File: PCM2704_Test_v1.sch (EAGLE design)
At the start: 50 parts, among them IC1 REG1117, IC2 REG1117, X1 USB-MB-S

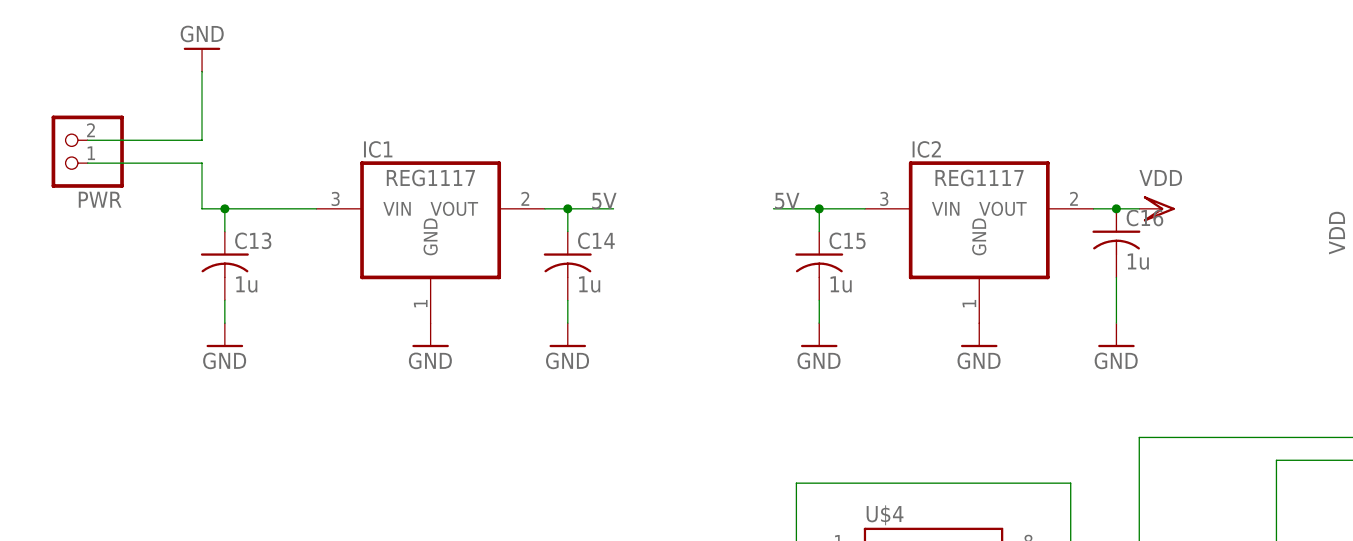
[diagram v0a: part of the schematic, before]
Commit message: Removed Voltage Regulators
For VBUS operation, no voltage regulators are required. I removed both
of them from the board along with all supporting components such as
filter caps, etc.
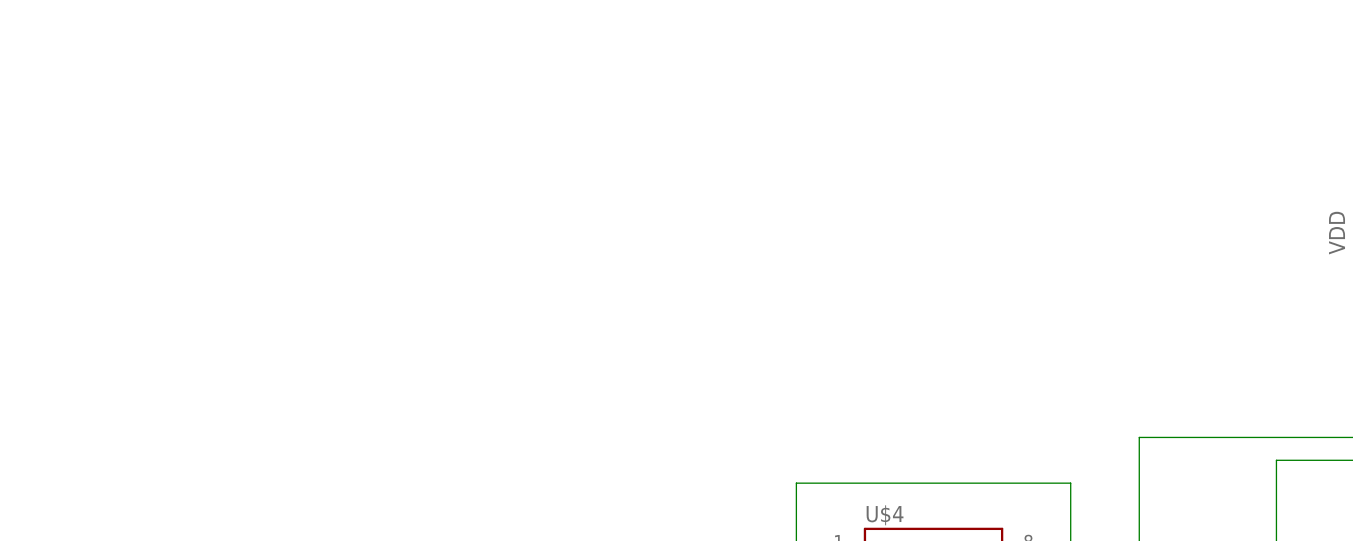
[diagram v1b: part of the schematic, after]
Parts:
- removed C13, C14, C15, C16: 1u, rcl:C-USC0805
- removed IC1, IC2: REG1117, burr-brown-3:REG1117
- removed PWR: (no value), pinhead:PINHD-1X2
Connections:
- removed net VIN: C13.1, IC1.VIN, PWR.1
- net 5V: no longer C14.1, C15.1, IC1.VOUT, IC2.VIN
- net GND: no longer C13.2, C14.2, C15.2, C16.2, IC1.GND, IC2.GND, PWR.2
- net VDD: no longer C16.1, IC2.VOUT
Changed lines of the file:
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@@
 <setting verticaltext="up"/>
 </settings>
-<grid distance="0.1" unitdist="inch" unit="inch" style="lines" multiple="1" display="yes" altdistance="0.01" altunitdist="inch" altunit="inch"/>
+<grid distance="0.1" unitdist="inch" unit="inch" style="lines" multiple="1" display="no" altdistance="0.01" altunitdist="inch" altunit="inch"/>
 <layers>
 <layer number="1" name="Top" color="4" fill="1" visible="no" active="no"/>
@@
 <part name="U$2" library="SparkFun-Connectors" deviceset="AUDIO-JACK3" device=""/>
 <part name="GND8" library="SparkFun" deviceset="GND" device=""/>
-<part name="GND9" library="SparkFun" deviceset="GND" device=""/>
-<part name="GND10" library="SparkFun" deviceset="GND" device=""/>
-<part name="C13" library="rcl" deviceset="C-US" device="C0805" value="1u"/>
-<part name="GND11" library="SparkFun" deviceset="GND" device=""/>
-<part name="C14" library="rcl" deviceset="C-US" device="C0805" value="1u"/>
-<part name="GND12" library="SparkFun" deviceset="GND" device=""/>
-<part name="IC1" library="burr-brown-3" deviceset="REG1117" device=""/>
-<part name="IC2" library="burr-brown-3" deviceset="REG1117" device=""/>
-<part name="C15" library="rcl" deviceset="C-US" device="C0805" value="1u"/>
-<part name="GND13" library="SparkFun" deviceset="GND" device=""/>
-<part name="GND14" library="SparkFun" deviceset="GND" device=""/>
-<part name="VDD1" library="supply1" deviceset="VDD" device=""/>
-<part name="C16" library="rcl" deviceset="C-US" device="C0805" value="1u"/>
-<part name="GND15" library="SparkFun" deviceset="GND" device=""/>
-<part name="PWR" library="pinhead" deviceset="PINHD-1X2" device=""/>
 <part name="L1" library="rcl" deviceset="L-US" device="L3225M"/>
 <part name="JPBUS" library="pinhead" deviceset="PINHD-1X2" device=""/>
@@
 <instance part="U$2" gate="G$1" x="198.12" y="15.24" rot="MR0"/>
 <instance part="GND8" gate="1" x="190.5" y="-2.54"/>
-<instance part="GND9" gate="1" x="-101.6" y="114.3"/>
-<instance part="GND10" gate="1" x="-127" y="147.32" rot="R180"/>
-<instance part="C13" gate="G$1" x="-124.46" y="124.46"/>
-<instance part="GND11" gate="1" x="-124.46" y="114.3"/>
-<instance part="C14" gate="G$1" x="-86.36" y="124.46"/>
-<instance part="GND12" gate="1" x="-86.36" y="114.3"/>
-<instance part="IC1" gate="G$1" x="-101.6" y="129.54"/>
-<instance part="IC2" gate="G$1" x="-40.64" y="129.54"/>
-<instance part="C15" gate="G$1" x="-58.42" y="124.46"/>
-<instance part="GND13" gate="1" x="-58.42" y="114.3"/>
-<instance part="GND14" gate="1" x="-40.64" y="114.3"/>
-<instance part="VDD1" gate="G$1" x="-20.32" y="129.54" rot="R270"/>
-<instance part="C16" gate="G$1" x="-25.4" y="127"/>
-<instance part="GND15" gate="1" x="-25.4" y="114.3"/>
-<instance part="PWR" gate="G$1" x="-142.24" y="137.16" rot="R180"/>
 <instance part="L1" gate="G$1" x="-101.6" y="43.18" rot="R90"/>
 <instance part="JPBUS" gate="G$1" x="-139.7" y="71.12" rot="R180"/>
@@
 </segment>
 <segment>
-<pinref part="GND9" gate="1" pin="GND"/>
-<pinref part="IC1" gate="G$1" pin="GND"/>
-</segment>
-<segment>
-<wire x1="-127" y1="137.16" x2="-127" y2="144.78" width="0.1524" layer="91"/>
-<pinref part="GND10" gate="1" pin="GND"/>
-<pinref part="PWR" gate="G$1" pin="2"/>
-<wire x1="-139.7" y1="137.16" x2="-127" y2="137.16" width="0.1524" layer="91"/>
-</segment>
-<segment>
-<pinref part="C13" gate="G$1" pin="2"/>
-<pinref part="GND11" gate="1" pin="GND"/>
-<wire x1="-124.46" y1="116.84" x2="-124.46" y2="119.38" width="0.1524" layer="91"/>
-</segment>
-<segment>
-<pinref part="C14" gate="G$1" pin="2"/>
-<pinref part="GND12" gate="1" pin="GND"/>
-<wire x1="-86.36" y1="116.84" x2="-86.36" y2="119.38" width="0.1524" layer="91"/>
-</segment>
-<segment>
-<pinref part="C15" gate="G$1" pin="2"/>
-<pinref part="GND13" gate="1" pin="GND"/>
-<wire x1="-58.42" y1="116.84" x2="-58.42" y2="119.38" width="0.1524" layer="91"/>
-</segment>
-<segment>
-<pinref part="IC2" gate="G$1" pin="GND"/>
-<pinref part="GND14" gate="1" pin="GND"/>
-</segment>
-<segment>
-<pinref part="C16" gate="G$1" pin="2"/>
-<pinref part="GND15" gate="1" pin="GND"/>
-<wire x1="-25.4" y1="116.84" x2="-25.4" y2="121.92" width="0.1524" layer="91"/>
-</segment>
-<segment>
 <pinref part="R2" gate="G$1" pin="2"/>
 <pinref part="GND16" gate="1" pin="GND"/>
@@
 </net>
 <net name="VDD" class="0">
-<segment>
-<pinref part="IC2" gate="G$1" pin="VOUT"/>
-<pinref part="VDD1" gate="G$1" pin="VDD"/>
-<wire x1="-22.86" y1="129.54" x2="-25.4" y2="129.54" width="0.1524" layer="91"/>
-<pinref part="C16" gate="G$1" pin="1"/>
-<wire x1="-25.4" y1="129.54" x2="-27.94" y2="129.54" width="0.1524" layer="91"/>
-<junction x="-25.4" y="129.54"/>
-</segment>
 <segment>
 <wire x1="12.7" y1="43.18" x2="-15.24" y2="43.18" width="0.1524" layer="91"/>
@@
 </segment>
 </net>
-<net name="VIN" class="0">
-<segment>
-<wire x1="-127" y1="134.62" x2="-127" y2="129.54" width="0.1524" layer="91"/>
-<wire x1="-127" y1="129.54" x2="-124.46" y2="129.54" width="0.1524" layer="91"/>
-<wire x1="-124.46" y1="129.54" x2="-114.3" y2="129.54" width="0.1524" layer="91"/>
-<pinref part="C13" gate="G$1" pin="1"/>
-<wire x1="-124.46" y1="127" x2="-124.46" y2="129.54" width="0.1524" layer="91"/>
-<junction x="-124.46" y="129.54"/>
-<pinref part="IC1" gate="G$1" pin="VIN"/>
-<pinref part="PWR" gate="G$1" pin="1"/>
-<wire x1="-139.7" y1="134.62" x2="-127" y2="134.62" width="0.1524" layer="91"/>
-</segment>
-</net>
 <net name="5V" class="0">
 <segment>
-<wire x1="-88.9" y1="129.54" x2="-86.36" y2="129.54" width="0.1524" layer="91"/>
-<pinref part="C14" gate="G$1" pin="1"/>
-<wire x1="-86.36" y1="129.54" x2="-81.28" y2="129.54" width="0.1524" layer="91"/>
-<wire x1="-86.36" y1="129.54" x2="-86.36" y2="127" width="0.1524" layer="91"/>
-<junction x="-86.36" y="129.54"/>
-<pinref part="IC1" gate="G$1" pin="VOUT"/>
-<label x="-83.82" y="129.54" size="1.778" layer="95"/>
-</segment>
-<segment>
-<pinref part="IC2" gate="G$1" pin="VIN"/>
-<wire x1="-63.5" y1="129.54" x2="-58.42" y2="129.54" width="0.1524" layer="91"/>
-<label x="-63.5" y="129.54" size="1.778" layer="95"/>
-<pinref part="C15" gate="G$1" pin="1"/>
-<wire x1="-58.42" y1="129.54" x2="-53.34" y2="129.54" width="0.1524" layer="91"/>
-<wire x1="-58.42" y1="127" x2="-58.42" y2="129.54" width="0.1524" layer="91"/>
-<junction x="-58.42" y="129.54"/>
-</segment>
-<segment>
 <pinref part="JPBUS" gate="G$1" pin="2"/>

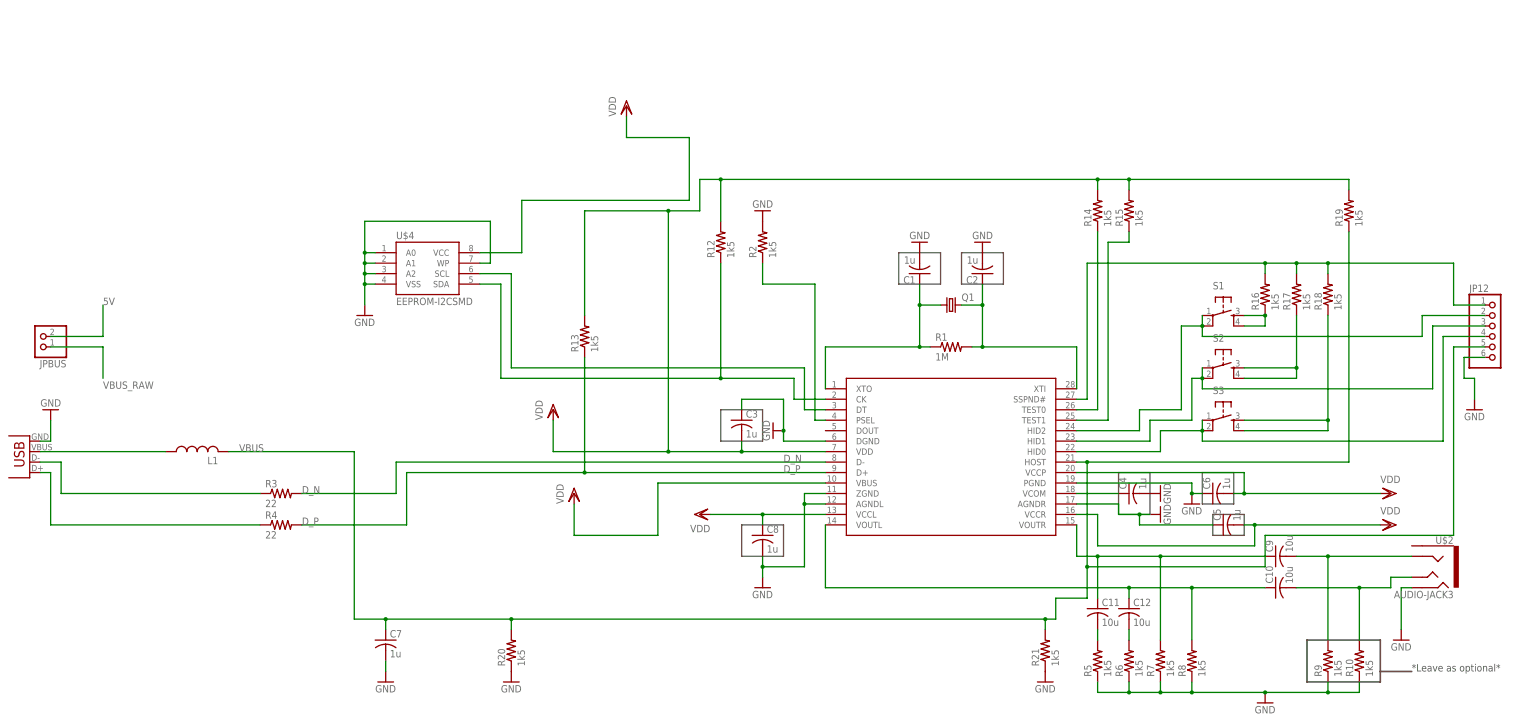
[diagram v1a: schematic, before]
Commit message: Removed unnecessary components
Removed:
-  Function Buttons
-  Resistors associated with the buttons

Moved some components around to make better use of the space on the
board. Decreased the board length and width. Routed the EEPROM traces
and added a bypass capacitor footprint to the power pin of the EEPROM.

Ripped up some traces and instead used polygon pours to route the
signals to make them lower impedance traces. This includes the traces
routed to the headphone jack and the USB VBUS pin.
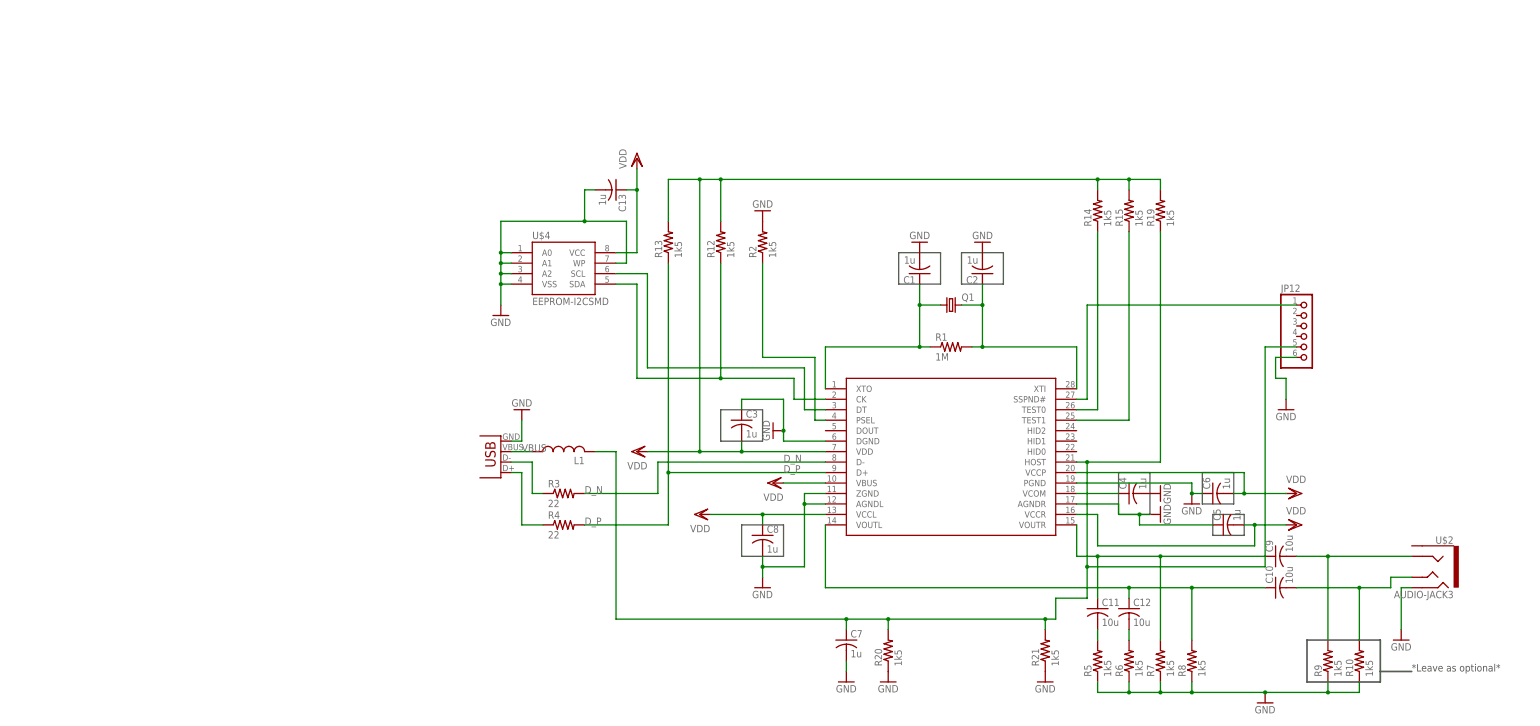
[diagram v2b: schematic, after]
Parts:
- removed JPBUS: (no value), pinhead:PINHD-1X2
- removed R16, R17, R18: 1k5, rcl:R-US_R0603
- removed S1, S2, S3: (no value), SparkFun:TAC_SWITCHSMD
- added C13: 1u, rcl:C-USC0402
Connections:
- removed net 5V: JPBUS.2
- removed net N$10: R17.1, S2.3, S2.4
- removed net N$11: R18.1, S3.3, S3.4
- removed net N$22: JP12.4, S3.1, S3.2, U$1.HID0
- removed net N$23: JP12.3, S2.1, S2.2, U$1.HID1
- removed net N$24: JP12.2, S1.1, S1.2, U$1.HID2
- removed net N$8: R16.1, S1.3, S1.4
- net GND: now also C13.2
- net SSPND: no longer R16.2, R17.2, R18.2
- net VBUS_RAW: no longer JPBUS.1
- net VDD: now also C13.1
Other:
- moved on the sheet: C7, JP12, L1, R13, R19, R20, R3, R4, U$4

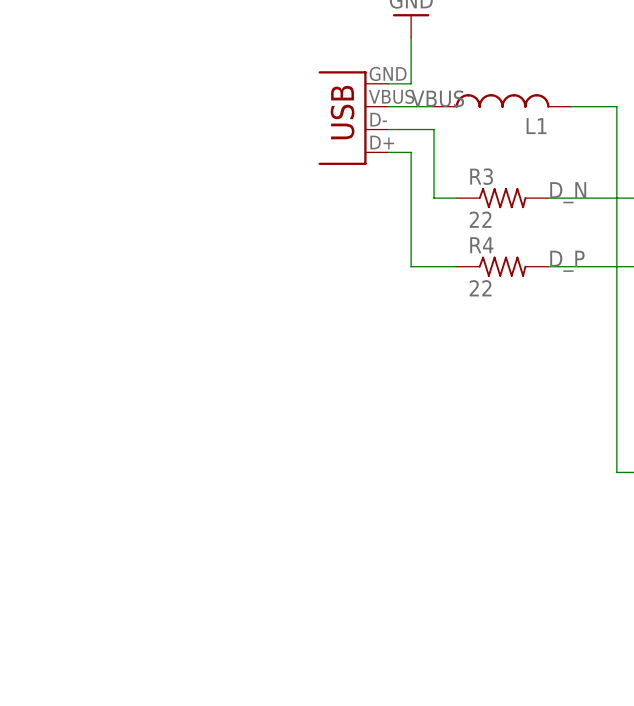
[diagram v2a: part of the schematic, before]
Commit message: Added LDO for Self-Power
Added an LDO to this design for self-powering the board.
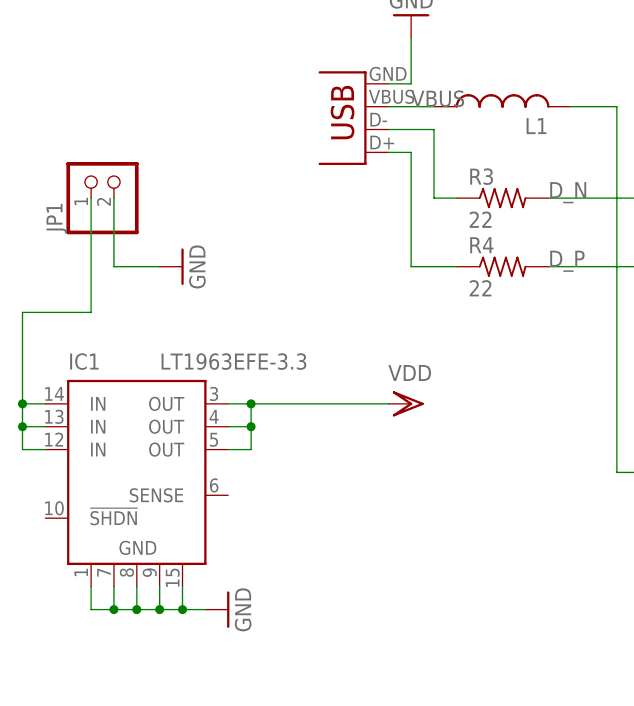
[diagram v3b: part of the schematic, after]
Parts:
- added IC1: LT1963EFE-3.3, linear-technology:LT1963EFE-3.3
- added JP1: (no value), pinhead:PINHD-1X2
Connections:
- new net N$3: IC1.IN@1, IC1.IN@2, IC1.IN@3, JP1.1
- net GND: now also IC1.GND@1, IC1.GND@2, IC1.GND@3, IC1.GND@4, IC1.GND@5, JP1.2
- net VDD: now also IC1.OUT@1, IC1.OUT@2, IC1.OUT@3
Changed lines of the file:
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@@
 <part name="R12" library="rcl" deviceset="R-US_" device="R0603" value="1k5"/>
 <part name="C13" library="rcl" deviceset="C-US" device="C0402" value="1u"/>
+<part name="IC1" library="linear-technology" deviceset="LT1963EFE" device="" technology="-3.3"/>
+<part name="JP1" library="pinhead" deviceset="PINHD-1X2" device=""/>
+<part name="GND9" library="SparkFun" deviceset="GND" device=""/>
+<part name="VDD1" library="supply1" deviceset="VDD" device=""/>
+<part name="GND10" library="SparkFun" deviceset="GND" device=""/>
 </parts>
 <sheets>
@@
 <instance part="R12" gate="G$1" x="25.4" y="93.98" rot="R90"/>
 <instance part="C13" gate="G$1" x="0" y="106.68" rot="R270"/>
+<instance part="IC1" gate="G$1" x="-53.34" y="7.62"/>
+<instance part="JP1" gate="G$1" x="-55.88" y="35.56" rot="R90"/>
+<instance part="GND9" gate="1" x="-48.26" y="25.4" rot="R90"/>
+<instance part="VDD1" gate="G$1" x="-22.86" y="10.16" rot="R270"/>
+<instance part="GND10" gate="1" x="-43.18" y="-12.7" rot="R90"/>
 </instances>
 <busses>
@@
 <wire x1="-7.62" y1="106.68" x2="-7.62" y2="99.06" width="0.1524" layer="91"/>
 <junction x="-7.62" y="99.06"/>
+</segment>
+<segment>
+<pinref part="JP1" gate="G$1" pin="2"/>
+<wire x1="-55.88" y1="33.02" x2="-55.88" y2="25.4" width="0.1524" layer="91"/>
+<wire x1="-55.88" y1="25.4" x2="-50.8" y2="25.4" width="0.1524" layer="91"/>
+<pinref part="GND9" gate="1" pin="GND"/>
+</segment>
+<segment>
+<pinref part="IC1" gate="G$1" pin="GND@1"/>
+<wire x1="-58.42" y1="-10.16" x2="-58.42" y2="-12.7" width="0.1524" layer="91"/>
+<pinref part="GND10" gate="1" pin="GND"/>
+<wire x1="-58.42" y1="-12.7" x2="-55.88" y2="-12.7" width="0.1524" layer="91"/>
+<pinref part="IC1" gate="G$1" pin="GND@2"/>
+<wire x1="-55.88" y1="-12.7" x2="-53.34" y2="-12.7" width="0.1524" layer="91"/>
+<wire x1="-53.34" y1="-12.7" x2="-50.8" y2="-12.7" width="0.1524" layer="91"/>
+<wire x1="-50.8" y1="-12.7" x2="-48.26" y2="-12.7" width="0.1524" layer="91"/>
+<wire x1="-48.26" y1="-12.7" x2="-45.72" y2="-12.7" width="0.1524" layer="91"/>
+<wire x1="-55.88" y1="-10.16" x2="-55.88" y2="-12.7" width="0.1524" layer="91"/>
+<junction x="-55.88" y="-12.7"/>
+<pinref part="IC1" gate="G$1" pin="GND@3"/>
+<wire x1="-53.34" y1="-10.16" x2="-53.34" y2="-12.7" width="0.1524" layer="91"/>
+<junction x="-53.34" y="-12.7"/>
+<pinref part="IC1" gate="G$1" pin="GND@4"/>
+<wire x1="-50.8" y1="-10.16" x2="-50.8" y2="-12.7" width="0.1524" layer="91"/>
+<junction x="-50.8" y="-12.7"/>
+<pinref part="IC1" gate="G$1" pin="GND@5"/>
+<wire x1="-48.26" y1="-10.16" x2="-48.26" y2="-12.7" width="0.1524" layer="91"/>
+<junction x="-48.26" y="-12.7"/>
 </segment>
 </net>
@@
 <pinref part="U$1" gate="G$1" pin="VBUS"/>
 <wire x1="40.64" y1="35.56" x2="50.8" y2="35.56" width="0.1524" layer="91"/>
+</segment>
+<segment>
+<pinref part="IC1" gate="G$1" pin="OUT@1"/>
+<wire x1="-43.18" y1="10.16" x2="-40.64" y2="10.16" width="0.1524" layer="91"/>
+<pinref part="VDD1" gate="G$1" pin="VDD"/>
+<pinref part="IC1" gate="G$1" pin="OUT@3"/>
+<wire x1="-40.64" y1="10.16" x2="-25.4" y2="10.16" width="0.1524" layer="91"/>
+<wire x1="-43.18" y1="5.08" x2="-40.64" y2="5.08" width="0.1524" layer="91"/>
+<wire x1="-40.64" y1="5.08" x2="-40.64" y2="7.62" width="0.1524" layer="91"/>
+<junction x="-40.64" y="10.16"/>
+<pinref part="IC1" gate="G$1" pin="OUT@2"/>
+<wire x1="-40.64" y1="7.62" x2="-40.64" y2="10.16" width="0.1524" layer="91"/>
+<wire x1="-43.18" y1="7.62" x2="-40.64" y2="7.62" width="0.1524" layer="91"/>
+<junction x="-40.64" y="7.62"/>
 </segment>
 </net>
@@
 </segment>
 </net>
+<net name="N$3" class="0">
+<segment>
+<pinref part="JP1" gate="G$1" pin="1"/>
+<wire x1="-58.42" y1="33.02" x2="-58.42" y2="20.32" width="0.1524" layer="91"/>
+<wire x1="-58.42" y1="20.32" x2="-66.04" y2="20.32" width="0.1524" layer="91"/>
+<wire x1="-66.04" y1="20.32" x2="-66.04" y2="10.16" width="0.1524" layer="91"/>
+<pinref part="IC1" gate="G$1" pin="IN@3"/>
+<wire x1="-66.04" y1="10.16" x2="-66.04" y2="7.62" width="0.1524" layer="91"/>
+<wire x1="-66.04" y1="7.62" x2="-66.04" y2="5.08" width="0.1524" layer="91"/>
+<wire x1="-66.04" y1="5.08" x2="-63.5" y2="5.08" width="0.1524" layer="91"/>
+<pinref part="IC1" gate="G$1" pin="IN@2"/>
+<wire x1="-63.5" y1="7.62" x2="-66.04" y2="7.62" width="0.1524" layer="91"/>
+<junction x="-66.04" y="7.62"/>
+<pinref part="IC1" gate="G$1" pin="IN@1"/>
+<wire x1="-63.5" y1="10.16" x2="-66.04" y2="10.16" width="0.1524" layer="91"/>
+<junction x="-66.04" y="10.16"/>
+</segment>
+</net>
